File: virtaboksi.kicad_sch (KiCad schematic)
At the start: 22 parts, among them J1 Conn_01x02_Female, J2 Conn_01x03_Female, J3 Conn_01x02_Female, J4 Conn_01x02_Female, J5 Conn_01x02_Female, J6 Conn_01x02_Female, J7 Conn_01x02_Female, Q1 IRF9540N, Q2 IRF9540N, Q3 IRF9540N

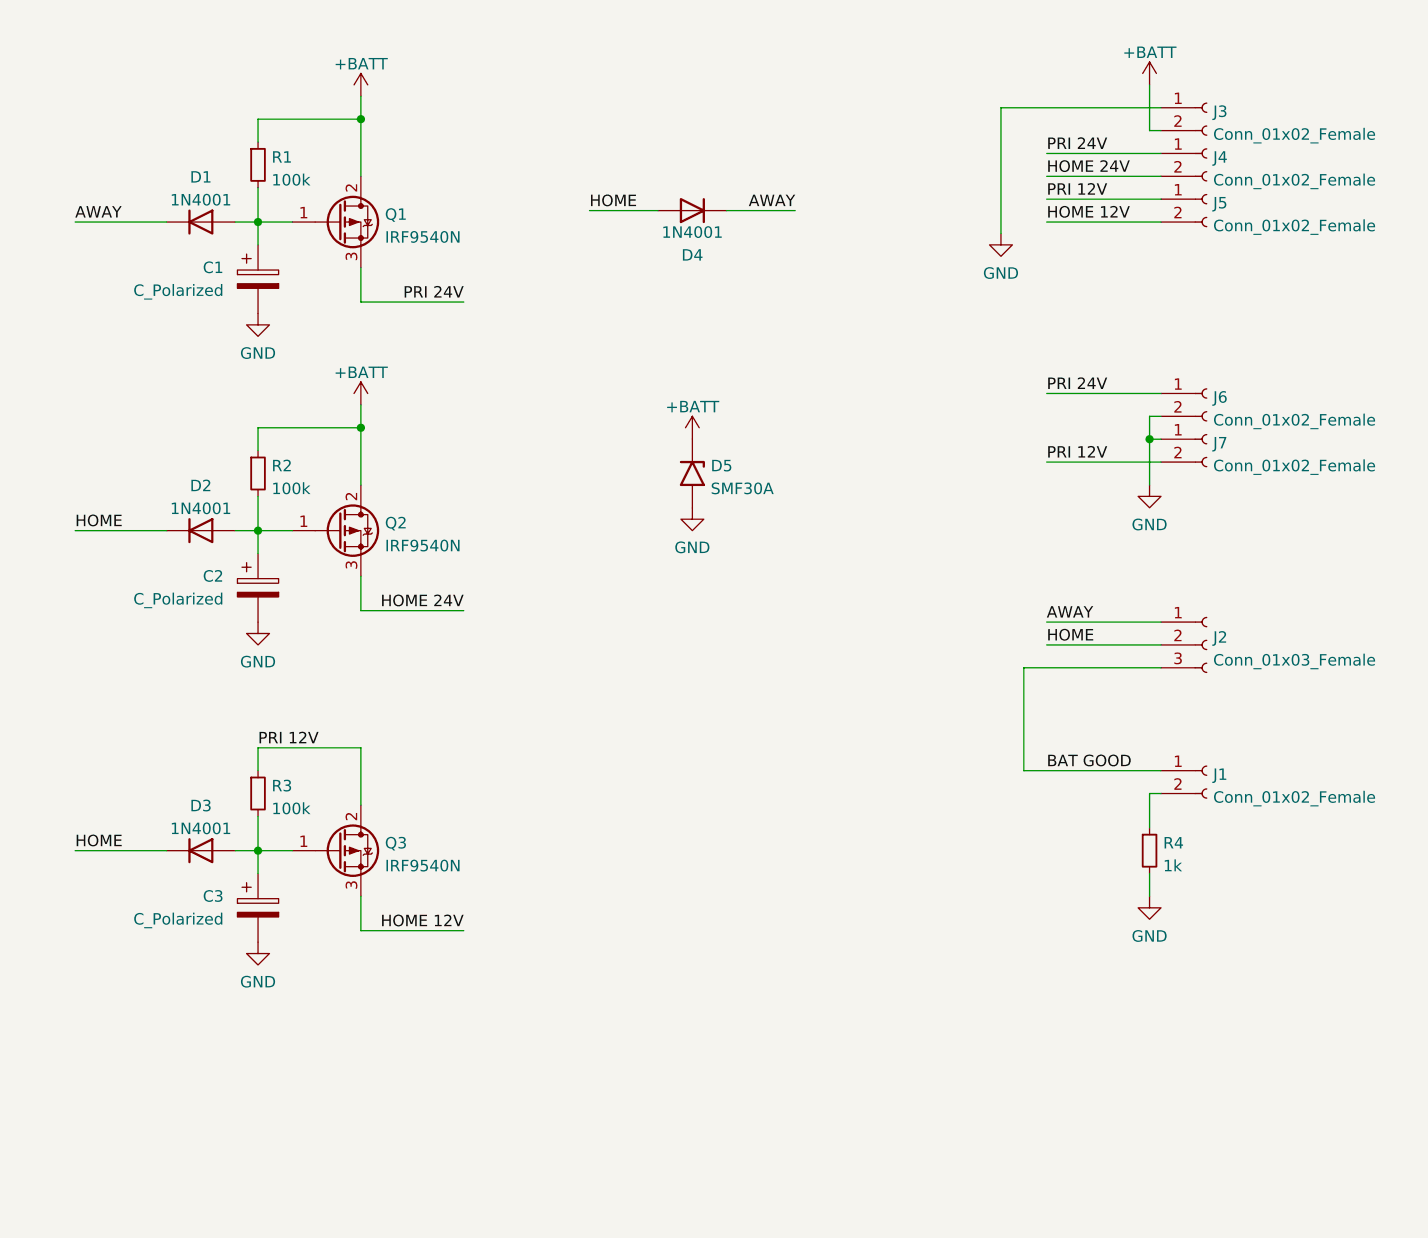
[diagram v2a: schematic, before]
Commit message: MOSFET drain and source were flipped
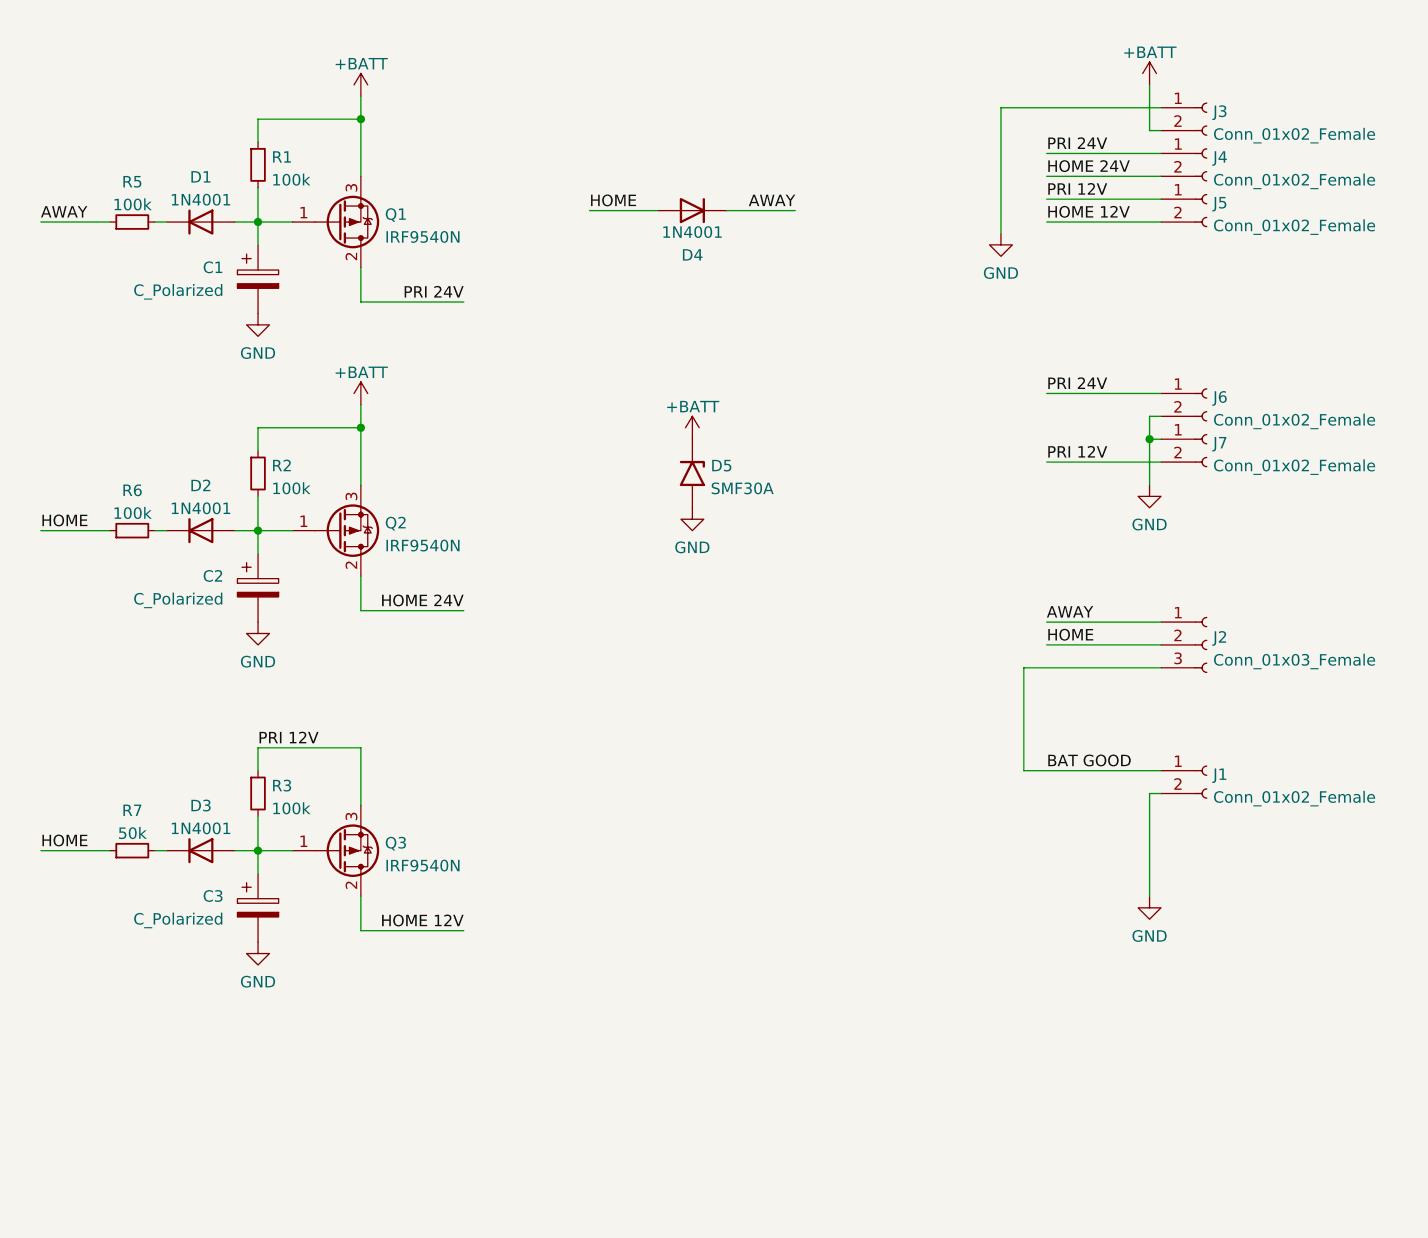
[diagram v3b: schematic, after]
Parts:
- removed R4: 1k, Resistor_THT:R_Axial_DIN0204_L3.6mm_D1.6mm_P2.54mm_Vertical, symbol Device:R_Small
- added R5, R6: 100k, Resistor_THT:R_Axial_DIN0204_L3.6mm_D1.6mm_P2.54mm_Vertical, symbol Device:R_Small
- added R7: 50k, Resistor_THT:R_Axial_DIN0204_L3.6mm_D1.6mm_P2.54mm_Vertical, symbol Device:R_Small
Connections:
- net +BATT: now also Q1.3 (S), Q2.3 (S); no longer Q1.2 (D), Q2.2 (D)
- net AWAY: now also R5.1; no longer D1.1 (K)
- net GND: now also J1.2 (Pin_2)
- net HOME: now also R6.1, R7.1; no longer D2.1 (K), D3.1 (K)
- net HOME 12V: now also Q3.2 (D); no longer Q3.3 (S)
- net HOME 24V: now also Q2.2 (D); no longer Q2.3 (S)
- net PRI 12V: now also Q3.3 (S); no longer Q3.2 (D)
- net PRI 24V: now also Q1.2 (D); no longer Q1.3 (S)
- new net: D1.1 (K), R5.2
- new net: D2.1 (K), R6.2
- new net: D3.1 (K), R7.2
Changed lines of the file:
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@@
     (stroke (width 0) (type default) (color 0 0 0 0))
   )
-  (wire (pts (xy 44.45 83.82) (xy 54.61 83.82))
+  (wire (pts (xy 53.34 119.38) (xy 54.61 119.38))
     (stroke (width 0) (type default) (color 0 0 0 0))
   )
@@
     (stroke (width 0) (type default) (color 0 0 0 0))
   )
-  (wire (pts (xy 44.45 119.38) (xy 54.61 119.38))
+  (wire (pts (xy 40.64 119.38) (xy 48.26 119.38))
     (stroke (width 0) (type default) (color 0 0 0 0))
   )
@@
     (stroke (width 0) (type default) (color 0 0 0 0))
   )
+  (wire (pts (xy 40.64 83.82) (xy 48.26 83.82))
+    (stroke (width 0) (type default) (color 0 0 0 0))
+  )
   (wire (pts (xy 64.77 49.53) (xy 64.77 45.72))
     (stroke (width 0) (type default) (color 0 0 0 0))
@@
     (stroke (width 0) (type default) (color 0 0 0 0))
   )
+  (wire (pts (xy 53.34 83.82) (xy 54.61 83.82))
+    (stroke (width 0) (type default) (color 0 0 0 0))
+  )
   (wire (pts (xy 68.58 49.53) (xy 64.77 49.53))
     (stroke (width 0) (type default) (color 0 0 0 0))
@@
     (stroke (width 0) (type default) (color 0 0 0 0))
   )
-  (wire (pts (xy 163.83 121.92) (xy 163.83 124.46))
-    (stroke (width 0) (type default) (color 0 0 0 0))
-  )
   (wire (pts (xy 76.2 72.39) (xy 76.2 78.74))
     (stroke (width 0) (type default) (color 0 0 0 0))
@@
     (stroke (width 0) (type default) (color 0 0 0 0))
   )
-  (wire (pts (xy 163.83 113.03) (xy 163.83 116.84))
+  (wire (pts (xy 163.83 113.03) (xy 163.83 124.46))
     (stroke (width 0) (type default) (color 0 0 0 0))
   )
@@
     (stroke (width 0) (type default) (color 0 0 0 0))
   )
-  (wire (pts (xy 44.45 49.53) (xy 54.61 49.53))
+  (wire (pts (xy 40.64 49.53) (xy 48.26 49.53))
     (stroke (width 0) (type default) (color 0 0 0 0))
   )
@@
     (stroke (width 0) (type default) (color 0 0 0 0))
   )
+  (wire (pts (xy 53.34 49.53) (xy 54.61 49.53))
+    (stroke (width 0) (type default) (color 0 0 0 0))
+  )
   (wire (pts (xy 87.63 92.71) (xy 76.2 92.71))
     (stroke (width 0) (type default) (color 0 0 0 0))
@@
     (effects (font (size 1.27 1.27)) (justify left bottom))
   )
-  (label "AWAY" (at 44.45 49.53 0)
+  (label "AWAY" (at 40.64 49.53 0)
     (effects (font (size 1.27 1.27)) (justify left bottom))
   )
@@
     (effects (font (size 1.27 1.27)) (justify left bottom))
   )
-  (label "HOME" (at 44.45 83.82 0)
+  (label "HOME" (at 40.64 83.82 0)
     (effects (font (size 1.27 1.27)) (justify left bottom))
   )
@@
     (effects (font (size 1.27 1.27)) (justify left bottom))
   )
-  (label "HOME" (at 44.45 119.38 0)
+  (label "HOME" (at 40.64 119.38 0)
     (effects (font (size 1.27 1.27)) (justify left bottom))
   )
@@
     (pin "2")
   )
+  (symbol (lib_id "Device:R_Small") (at 50.8 83.82 90) (unit 1)
+    (in_bom yes) (on_board yes) (fields_autoplaced)
+    (property "Reference" "R6" (id 0) (at 50.8 79.3836 90))
+    (property "Value" "100k" (id 1) (at 50.8 81.9205 90))
+    (property "Footprint" "Resistor_THT:R_Axial_DIN0204_L3.6mm_D1.6mm_P2.54mm_Vertical" (id 2) (at 50.8 83.82 0)
+      (effects (font (size 1.27 1.27)) hide)
+    )
+    (property "Datasheet" "~" (id 3) (at 50.8 83.82 0)
+      (effects (font (size 1.27 1.27)) hide)
+    )
+    (pin "1")
+    (pin "2")
+  )
   (symbol (lib_id "Device:R_Small") (at 64.77 43.18 0) (unit 1)
     (in_bom yes) (on_board yes) (fields_autoplaced)
@@
     (pin "3")
   )
-  (symbol (lib_id "Device:R_Small") (at 163.83 119.38 0) (unit 1)
-    (in_bom yes) (on_board yes) (fields_autoplaced)
-    (property "Reference" "R4" (id 0) (at 165.3286 118.5453 0)
-      (effects (font (size 1.27 1.27)) (justify left))
-    )
-    (property "Value" "1k" (id 1) (at 165.3286 121.0822 0)
-      (effects (font (size 1.27 1.27)) (justify left))
-    )
-    (property "Footprint" "Resistor_THT:R_Axial_DIN0204_L3.6mm_D1.6mm_P2.54mm_Vertical" (id 2) (at 163.83 119.38 0)
-      (effects (font (size 1.27 1.27)) hide)
-    )
-    (property "Datasheet" "~" (id 3) (at 163.83 119.38 0)
-      (effects (font (size 1.27 1.27)) hide)
-    )
-    (pin "1")
-    (pin "2")
-  )
-  (symbol (lib_id "Transistor_FET:IRF9540N") (at 73.66 49.53 0) (unit 1)
+  (symbol (lib_id "Transistor_FET:IRF9540N") (at 73.66 49.53 0) (mirror x) (unit 1)
     (in_bom yes) (on_board yes) (fields_autoplaced)
     (property "Reference" "Q1" (id 0) (at 78.867 48.6953 0)
@@
       (effects (font (size 1.27 1.27)) (justify left))
     )
-    (property "Footprint" "Package_TO_SOT_THT:TO-220-3_Vertical" (id 2) (at 78.74 51.435 0)
+    (property "Footprint" "Package_TO_SOT_THT:TO-220-3_Vertical" (id 2) (at 78.74 47.625 0)
       (effects (font (size 1.27 1.27) italic) (justify left) hide)
     )
@@
     (pin "2")
   )
-  (symbol (lib_id "Transistor_FET:IRF9540N") (at 73.66 83.82 0) (unit 1)
+  (symbol (lib_id "Transistor_FET:IRF9540N") (at 73.66 83.82 0) (mirror x) (unit 1)
     (in_bom yes) (on_board yes) (fields_autoplaced)
     (property "Reference" "Q2" (id 0) (at 78.867 82.9853 0)
@@
       (effects (font (size 1.27 1.27)) (justify left))
     )
-    (property "Footprint" "Package_TO_SOT_THT:TO-220-3_Vertical" (id 2) (at 78.74 85.725 0)
+    (property "Footprint" "Package_TO_SOT_THT:TO-220-3_Vertical" (id 2) (at 78.74 81.915 0)
       (effects (font (size 1.27 1.27) italic) (justify left) hide)
     )
@@
     (pin "1")
   )
+  (symbol (lib_id "Device:R_Small") (at 50.8 119.38 90) (unit 1)
+    (in_bom yes) (on_board yes) (fields_autoplaced)
+    (property "Reference" "R7" (id 0) (at 50.8 114.9436 90))
+    (property "Value" "50k" (id 1) (at 50.8 117.4805 90))
+    (property "Footprint" "Resistor_THT:R_Axial_DIN0204_L3.6mm_D1.6mm_P2.54mm_Vertical" (id 2) (at 50.8 119.38 0)
+      (effects (font (size 1.27 1.27)) hide)
+    )
+    (property "Datasheet" "~" (id 3) (at 50.8 119.38 0)
+      (effects (font (size 1.27 1.27)) hide)
+    )
+    (pin "1")
+    (pin "2")
+  )
   (symbol (lib_id "power:GND") (at 163.83 124.46 0) (unit 1)
     (in_bom yes) (on_board yes) (fields_autoplaced)
@@
     (pin "2")
   )
-  (symbol (lib_id "Transistor_FET:IRF9540N") (at 73.66 119.38 0) (unit 1)
+  (symbol (lib_id "Transistor_FET:IRF9540N") (at 73.66 119.38 0) (mirror x) (unit 1)
     (in_bom yes) (on_board yes) (fields_autoplaced)
     (property "Reference" "Q3" (id 0) (at 78.867 118.5453 0)
@@
       (effects (font (size 1.27 1.27)) (justify left))
     )
-    (property "Footprint" "Package_TO_SOT_THT:TO-220-3_Vertical" (id 2) (at 78.74 121.285 0)
+    (property "Footprint" "Package_TO_SOT_THT:TO-220-3_Vertical" (id 2) (at 78.74 117.475 0)
       (effects (font (size 1.27 1.27) italic) (justify left) hide)
     )
@@
     )
     (pin "1")
+  )
+  (symbol (lib_id "Device:R_Small") (at 50.8 49.53 90) (unit 1)
+    (in_bom yes) (on_board yes) (fields_autoplaced)
+    (property "Reference" "R5" (id 0) (at 50.8 45.0936 90))
+    (property "Value" "100k" (id 1) (at 50.8 47.6305 90))
+    (property "Footprint" "Resistor_THT:R_Axial_DIN0204_L3.6mm_D1.6mm_P2.54mm_Vertical" (id 2) (at 50.8 49.53 0)
+      (effects (font (size 1.27 1.27)) hide)
+    )
+    (property "Datasheet" "~" (id 3) (at 50.8 49.53 0)
+      (effects (font (size 1.27 1.27)) hide)
+    )
+    (pin "1")
+    (pin "2")
   )
   (symbol (lib_id "power:+BATT") (at 113.03 73.66 0) (unit 1)
@@
       (reference "R3") (unit 1) (value "100k") (footprint "Resistor_THT:R_Axial_DIN0204_L3.6mm_D1.6mm_P2.54mm_Vertical")
     )
-    (path "/64f9f903-23c7-4e7e-a032-c3b8aca32034"
-      (reference "R4") (unit 1) (value "1k") (footprint "Resistor_THT:R_Axial_DIN0204_L3.6mm_D1.6mm_P2.54mm_Vertical")
-    )
-  )
+    (path "/d7b470dc-9ae6-4259-b9f7-328d930f92a1"
+      (reference "R5") (unit 1) (value "100k") (footprint "Resistor_THT:R_Axial_DIN0204_L3.6mm_D1.6mm_P2.54mm_Vertical")
+    )
+    (path "/4f9bda9e-f0c5-45b3-99bc-56bdb7bee83b"
+      (reference "R6") (unit 1) (value "100k") (footprint "Resistor_THT:R_Axial_DIN0204_L3.6mm_D1.6mm_P2.54mm_Vertical")
+    )
+    (path "/946b45c1-e02a-41b4-9a0a-d5d264adebb6"
+      (reference "R7") (unit 1) (value "50k") (footprint "Resistor_THT:R_Axial_DIN0204_L3.6mm_D1.6mm_P2.54mm_Vertical")
+    )
+  )

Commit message: Run the thing in Falstad's simulator and adjust the circuit
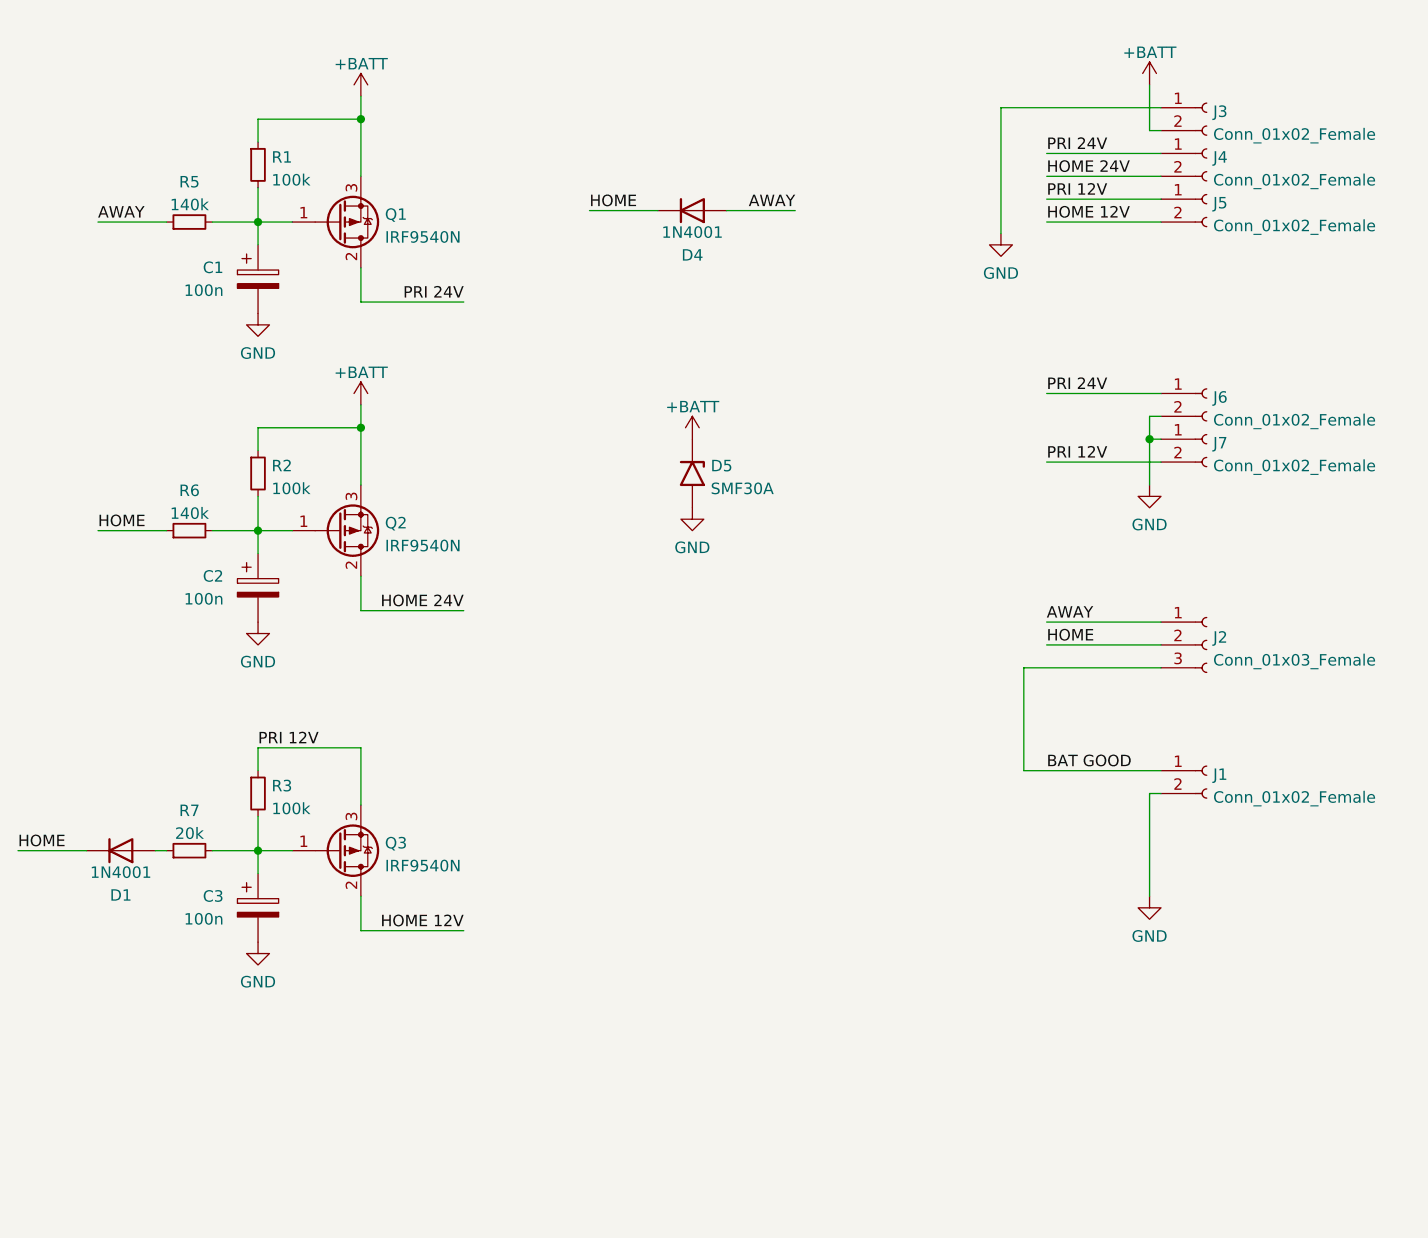
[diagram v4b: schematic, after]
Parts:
- removed D2, D3: 1N4001, Diode_THT:D_DO-41_SOD81_P10.16mm_Horizontal, symbol Diode:1N4001
- C1, C2, C3: value C_Polarized -> 100n
- R1, R2, R3: footprint Resistor_THT:R_Axial_DIN0204_L3.6mm_D1.6mm_P2.54mm_Vertical -> Resistor_THT:R_Axial_DIN0204_L3.6mm_D1.6mm_P5.08mm_Horizontal
- R5, R6: value 100k -> 140k; footprint Resistor_THT:R_Axial_DIN0204_L3.6mm_D1.6mm_P2.54mm_Vertical -> Resistor_THT:R_Axial_DIN0204_L3.6mm_D1.6mm_P5.08mm_Horizontal
- R7: value 50k -> 20k; footprint Resistor_THT:R_Axial_DIN0204_L3.6mm_D1.6mm_P2.54mm_Vertical -> Resistor_THT:R_Axial_DIN0204_L3.6mm_D1.6mm_P5.08mm_Horizontal
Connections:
- net AWAY: now also D4.2 (A); no longer D4.1 (K)
- net HOME: now also D1.1 (K), D4.1 (K); no longer D4.2 (A), R7.1
- net at C1.1, Q1.1 (G), R1.2: now also R5.2; no longer D1.2 (A)
- net at C2.1, Q2.1 (G), R2.2: now also R6.2
- net at R7.2: now also C3.1, Q3.1 (G), R3.2
- new net: D1.2 (A), R7.1
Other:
- moved on the sheet: D4, R5, R6, R7
